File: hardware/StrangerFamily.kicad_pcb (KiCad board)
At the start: 2 copper layers, 34.5 x 45.5 mm, 8 parts, among them J2 Power_LEDs, J3 Output_LEDs, P1 CONN_13X2, U1 TXB0104PW

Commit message: 2 channels, cleanup
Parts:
- removed C3, C4: 10u, Capacitor_SMD:C_0805_2012Metric_Pad1.15x1.40mm_HandSolder
- added J4: Output_LED_MOSI, Connector_JST:JST_XH_S03B-XH-A-1_1x03_P2.50mm_Horizontal, F.Cu at (151.2, 137.0)
- J3: value Output_LEDs -> Output_LED_PWM
- moved C1 21.8 mm to (164.5, 137.0)
- moved C2 21.8 mm to (164.5, 143.0)
- moved U1 21.8 mm to (158.8, 140.0)
- moved J2 16.1 mm to (148.5, 160.0), turned to 0 degrees
- moved J3 12.5 mm to (151.2, 148.0)
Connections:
- U1 pad 3: Net-(U1-Pad3) -> /GPIO10(MOSI)
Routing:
- net GND: track 98.8 -> 34.6 mm
- net /GPIO18: track 32.3 -> 9.97 mm
- net +3V3: track 39.2 -> 18.1 mm
- net VDD: track 34.0 -> 49.7 mm
- net /GPIO10(MOSI): track 0.00 -> 14.7 mm, vias 0 -> 1
- net Net-(J4-Pad2): track 0.00 -> 10.9 mm
- net +5V: track 13.2 -> 2.54 mm
- added copper zone on B.Cu, net GND
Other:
- outline, holes or cut-outs redrawn

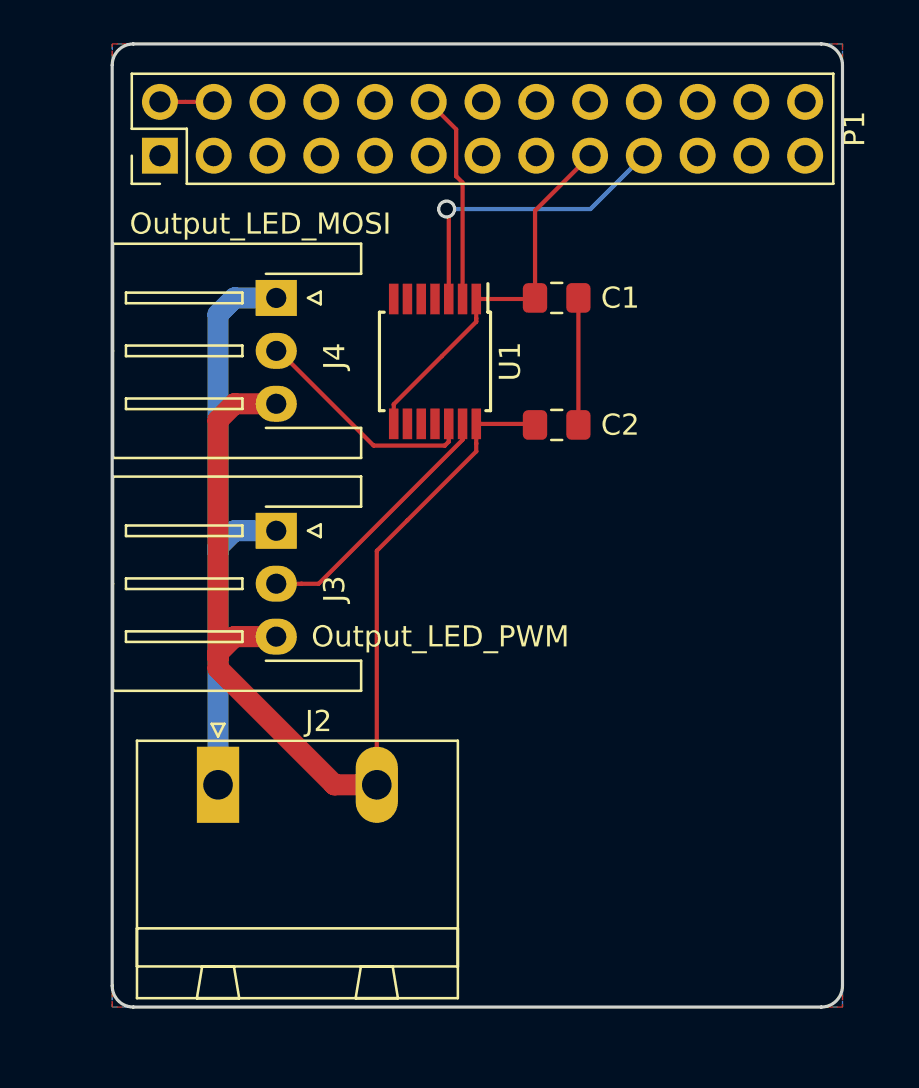
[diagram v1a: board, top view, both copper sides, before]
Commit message: Add LCD connector.
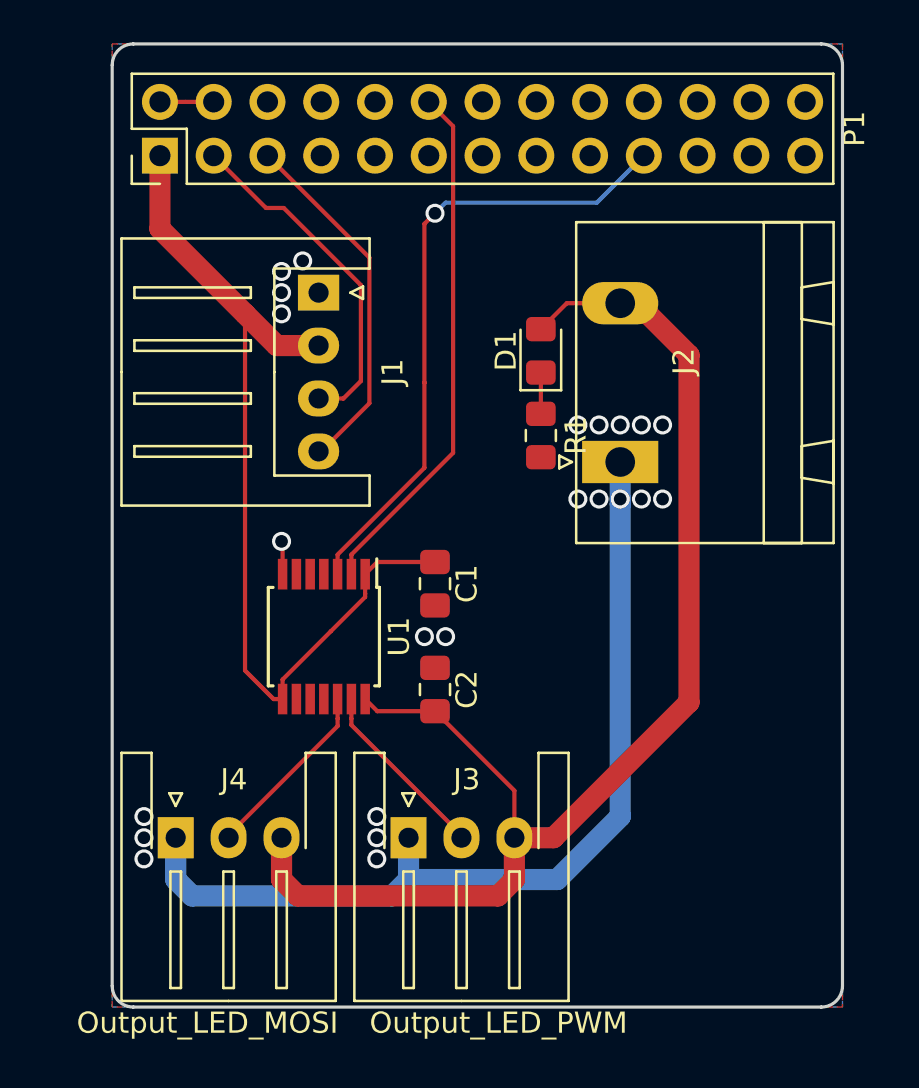
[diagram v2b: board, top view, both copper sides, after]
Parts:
- added D1: D, Diode_SMD:D_0805_2012Metric_Pad1.15x1.40mm_HandSolder, F.Cu at (163.8, 139.5)
- added J1: LCD_Conn, Connector_JST:JST_XH_S04B-XH-A_1x04_P2.50mm_Horizontal, F.Cu at (153.2, 136.8)
- added R1: R, Resistor_SMD:R_0805_2012Metric_Pad1.15x1.40mm_HandSolder, F.Cu at (163.8, 143.5)
- moved J4 25.9 mm to (146.5, 162.5), turned to 0 degrees
- moved J2 24.4 mm to (167.5, 144.8), turned to 90 degrees
- moved J3 15.8 mm to (157.5, 162.5), turned to 0 degrees
- moved C1 14.7 mm to (158.8, 150.5), turned to 90 degrees
- moved U1 14.0 mm to (153.5, 153.0)
- moved C2 13.8 mm to (158.8, 155.5), turned to 270 degrees
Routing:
- net +3V3: track 18.1 -> 43.5 mm
- net /GPIO1(SCL): track 0.00 -> 17.0 mm
- net /GPIO0(SDA): track 0.00 -> 16.4 mm
- net /GPIO10(MOSI): track 14.7 -> 29.9 mm
- net /GPIO18: track 9.97 -> 24.8 mm
- net VDD: track 49.7 -> 62.5 mm
- net GND: track 34.6 -> 45.1 mm, vias 0 -> 23
- net Net-(J3-Pad2): track 12.4 -> 8.70 mm
- net Net-(J4-Pad2): track 10.9 -> 8.68 mm
- net Net-(D1-Pad1): track 0.00 -> 1.95 mm

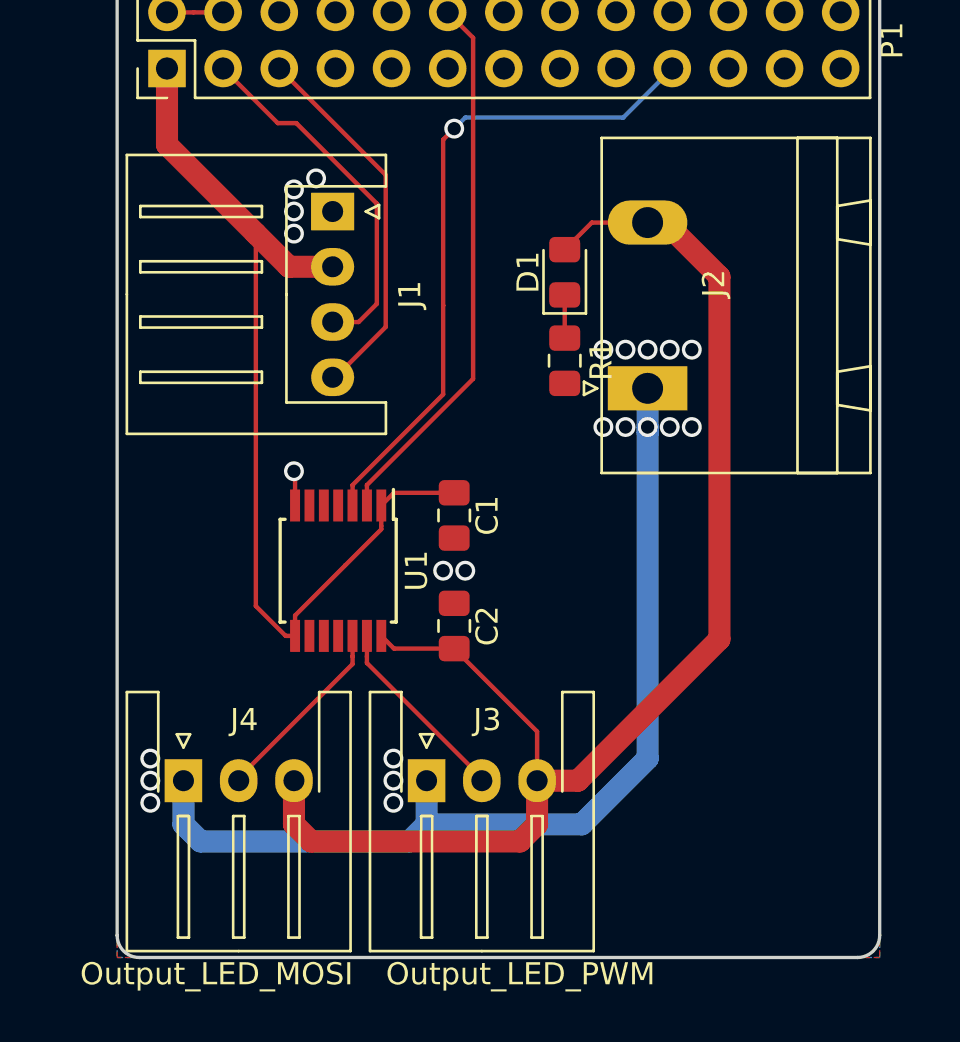
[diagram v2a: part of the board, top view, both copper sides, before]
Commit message: Change connector footprints (very small non critical changes)
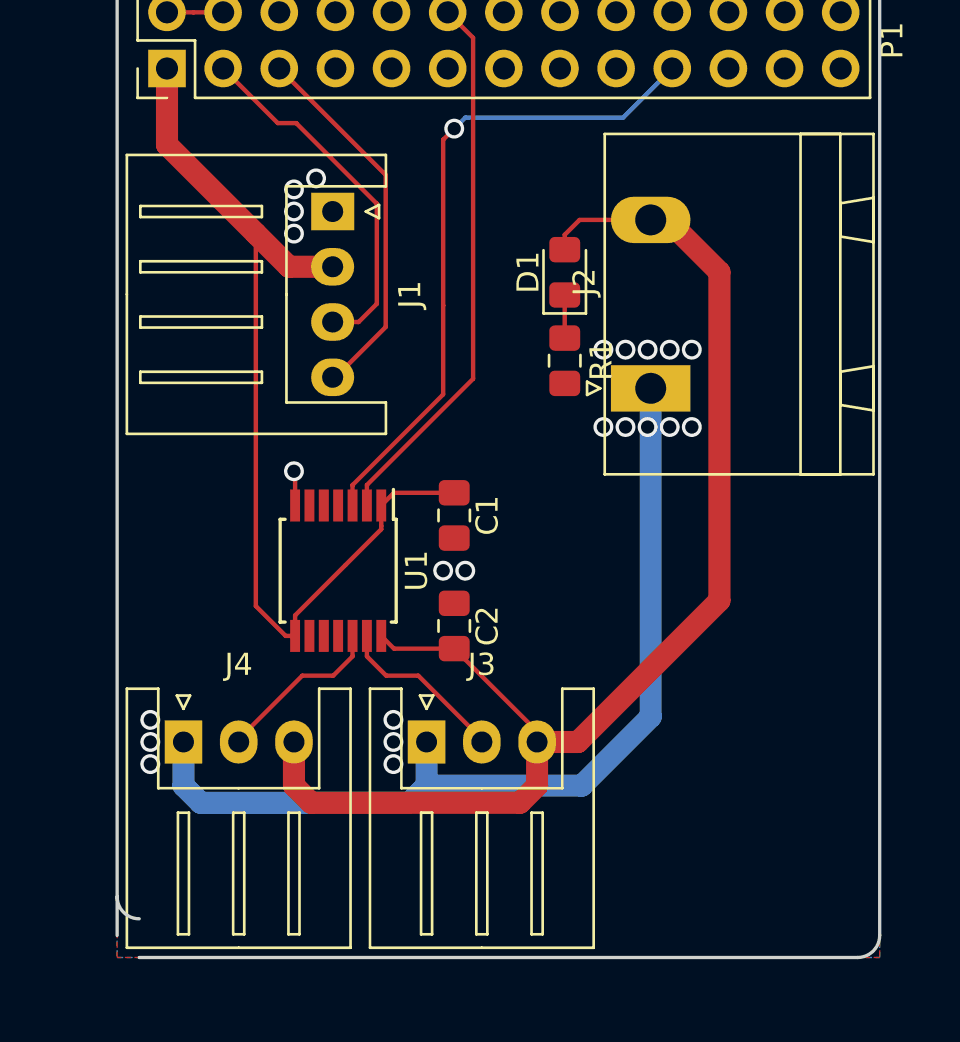
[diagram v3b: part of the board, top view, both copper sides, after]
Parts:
- J2: footprint Connector_Phoenix_GMSTB:PhoenixContact_GMSTBA_2,5_2-G_1x02_P7.50mm_Horizontal -> Connector_Phoenix_GMSTB:PhoenixContact_GMSTBA_2,5_2-G-7,62_1x02_P7.62mm_Horizontal
- J3, J4: footprint Connector_JST:JST_XH_S03B-XH-A-1_1x03_P2.50mm_Horizontal -> Connector_JST:JST_XH_S03B-XH-A_1x03_P2.50mm_Horizontal
- moved J3 1.75 mm to (157.5, 160.8)
- moved J4 1.75 mm to (146.5, 160.8)
- moved J2 0.14 mm to (167.6, 144.8)
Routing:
- net VDD: track 62.5 -> 59.6 mm
- net GND: track 45.1 -> 43.5 mm
- net Net-(J4-Pad2): track 8.68 -> 7.75 mm
- net Net-(J3-Pad2): track 8.70 -> 7.80 mm
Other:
- outline, holes or cut-outs redrawn

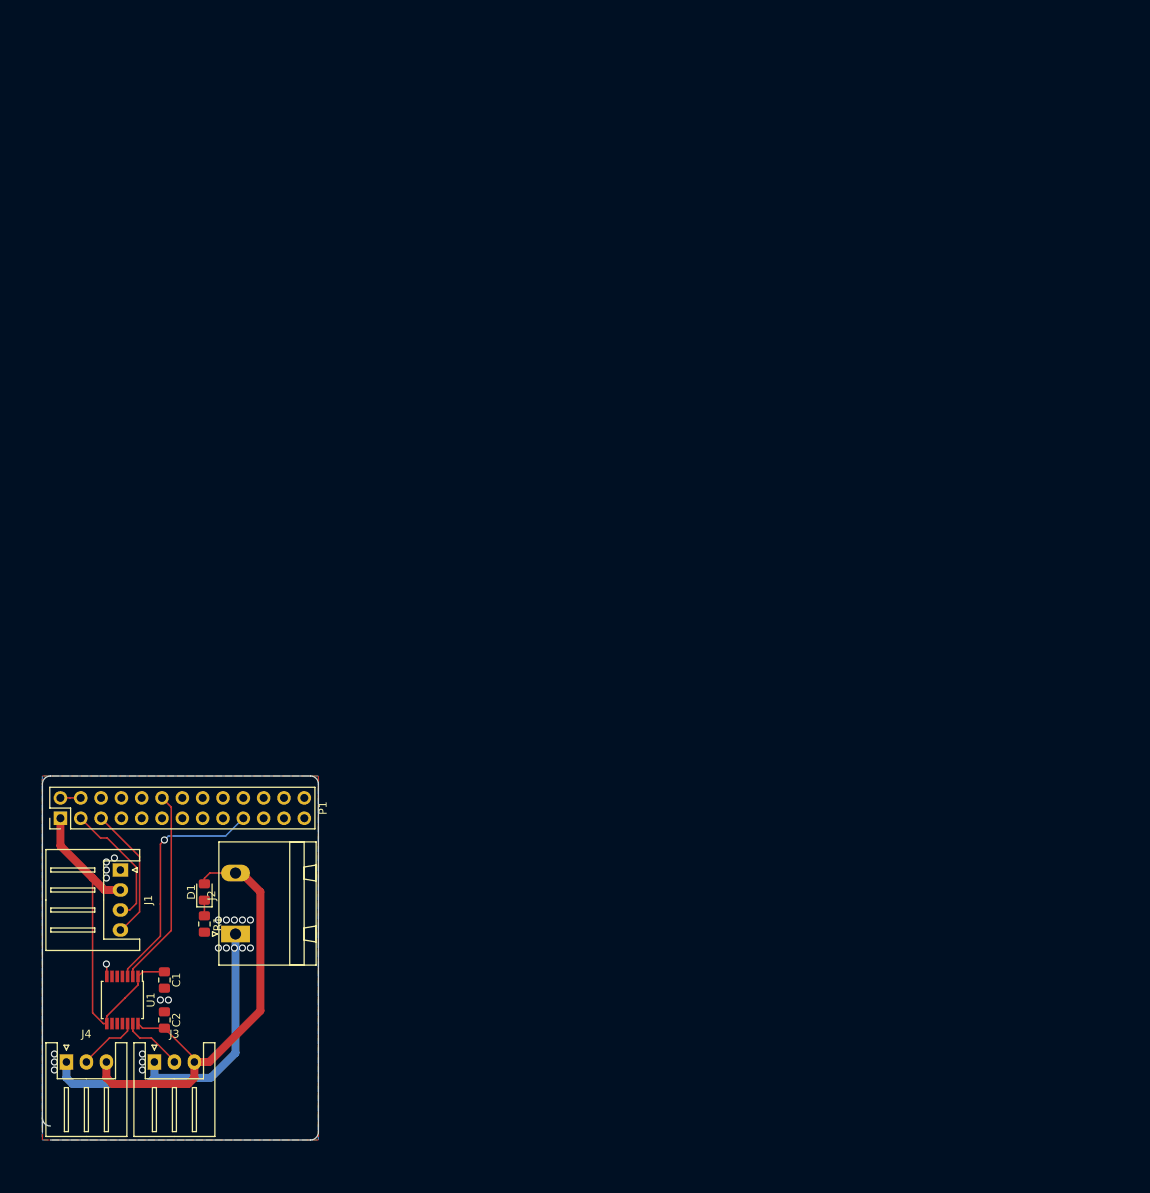
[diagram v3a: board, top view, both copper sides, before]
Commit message: v2 of hardware with rpi zero w, and arduino nano
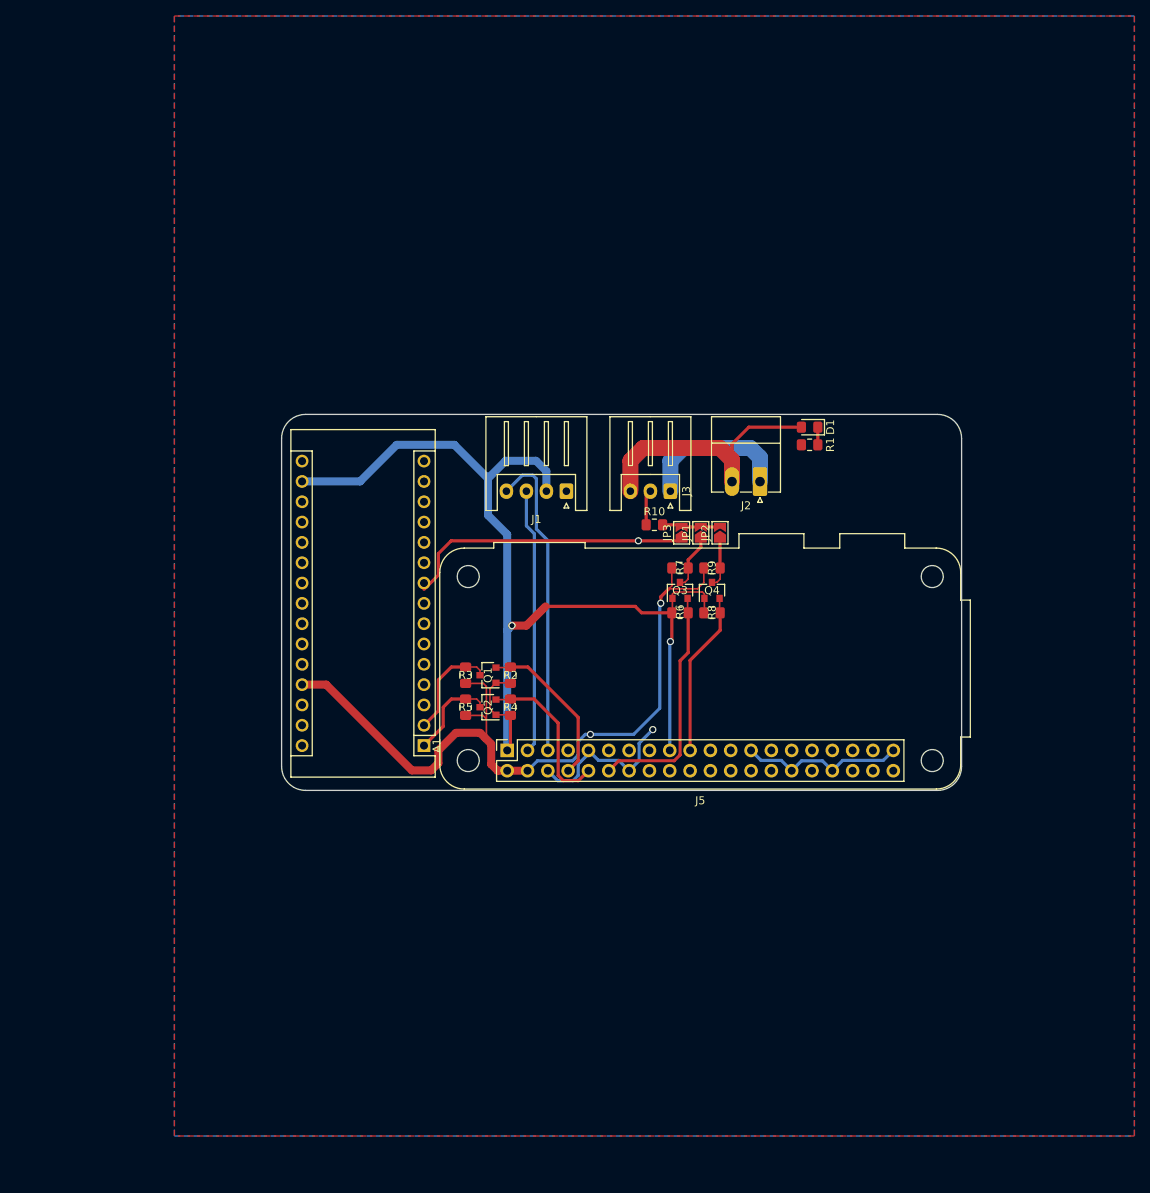
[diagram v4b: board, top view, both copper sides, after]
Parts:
- removed C1, C2: 100n, Capacitor_SMD:C_0805_2012Metric_Pad1.15x1.40mm_HandSolder
- removed J4: Output_LED_MOSI, Connector_JST:JST_XH_S03B-XH-A_1x03_P2.50mm_Horizontal
- removed P1: CONN_13X2, Connector_PinHeader_2.54mm:PinHeader_2x13_P2.54mm_Vertical
- removed U1: TXB0104PW, Package_SO:TSSOP-14_4.4x5mm_P0.65mm
- added A1: Arduino_Nano_v3.x, Module:Arduino_Nano, F.Cu at (191.2, 121.2)
- added J5: Raspberry_Pi_zero, Module:Raspberry_Pi_Zero_Socketed_THT_FaceDown_MountingHoles, F.Cu at (201.6, 121.8)
- added JP1: Jumper_NC, Jumper:SolderJumper-2_P1.3mm_Open_TrianglePad1.0x1.5mm, F.Cu at (225.8, 94.6)
- added JP2: Jumper_NC, Jumper:SolderJumper-2_P1.3mm_Open_TrianglePad1.0x1.5mm, F.Cu at (228.2, 94.6)
- added JP3: Jumper_NC, Jumper:SolderJumper-2_P1.3mm_Open_TrianglePad1.0x1.5mm, F.Cu at (223.4, 94.6)
- added Q1: BSS138, Package_TO_SOT_SMD:SOT-23, F.Cu at (199.2, 112.4)
- added Q2: BSS138, Package_TO_SOT_SMD:SOT-23, F.Cu at (199.2, 116.4)
- added Q3: BSS138, Package_TO_SOT_SMD:SOT-23, F.Cu at (223.2, 101.8)
- added Q4: BSS138, Package_TO_SOT_SMD:SOT-23, F.Cu at (227.2, 101.8)
- added R10: 470, Resistor_SMD:R_0805_2012Metric_Pad1.15x1.40mm_HandSolder, F.Cu at (220.0, 93.6)
- added R2: 10k, Resistor_SMD:R_0805_2012Metric_Pad1.15x1.40mm_HandSolder, F.Cu at (202.0, 112.4)
- added R3: 10k, Resistor_SMD:R_0805_2012Metric_Pad1.15x1.40mm_HandSolder, F.Cu at (196.4, 112.4)
- added R4: 10k, Resistor_SMD:R_0805_2012Metric_Pad1.15x1.40mm_HandSolder, F.Cu at (202.0, 116.4)
- added R5: 10k, Resistor_SMD:R_0805_2012Metric_Pad1.15x1.40mm_HandSolder, F.Cu at (196.4, 116.4)
- added R6: 10k, Resistor_SMD:R_0805_2012Metric_Pad1.15x1.40mm_HandSolder, F.Cu at (223.2, 104.6)
- added R7: 10k, Resistor_SMD:R_0805_2012Metric_Pad1.15x1.40mm_HandSolder, F.Cu at (223.2, 99.0)
- added R8: 10k, Resistor_SMD:R_0805_2012Metric_Pad1.15x1.40mm_HandSolder, F.Cu at (227.2, 104.6)
- added R9: 10k, Resistor_SMD:R_0805_2012Metric_Pad1.15x1.40mm_HandSolder, F.Cu at (227.2, 99.0)
- J1: footprint Connector_JST:JST_XH_S04B-XH-A_1x04_P2.50mm_Horizontal -> Connector_JST:JST_XH_S4B-XH-A_1x04_P2.50mm_Horizontal
- J2: footprint Connector_Phoenix_GMSTB:PhoenixContact_GMSTBA_2,5_2-G-7,62_1x02_P7.62mm_Horizontal -> Connector_Phoenix_MC:PhoenixContact_MC_1,5_2-G-3.5_1x02_P3.50mm_Horizontal
- J3: value Output_LED_PWM -> Output_LED; footprint Connector_JST:JST_XH_S03B-XH-A_1x03_P2.50mm_Horizontal -> Connector_JST:JST_XH_S3B-XH-A_1x03_P2.50mm_Horizontal
- moved R1 96.5 mm to (239.4, 83.6), turned to 180 degrees
- moved J3 96.2 mm to (222.0, 89.4), turned to 180 degrees
- moved D1 95.4 mm to (239.4, 81.4), turned to 180 degrees
- moved J2 86.6 mm to (233.2, 88.2), turned to 180 degrees
- moved J1 73.1 mm to (209.0, 89.4), turned to 180 degrees
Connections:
- J1 pad 3: /GPIO0(SDA) -> /LCD_SDA
- J1 pad 4: /GPIO1(SCL) -> /LCD_SLC
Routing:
- net +5V: track 2.54 -> 96.4 mm, vias 0 -> 2
- net +3V3: track 43.5 -> 134.4 mm, vias 0 -> 2
- net /LCD_SLC: track 0.00 -> 39.3 mm
- net /Arduino_out: track 0.00 -> 36.4 mm, vias 0 -> 1
- net /LCD_SDA: track 0.00 -> 33.2 mm
- net /GPIO10(MOSI): track 29.9 -> 0.00 mm, vias 1 -> 0
- net /PWM0: track 0.00 -> 29.7 mm
- net VDD: track 59.6 -> 32.0 mm
- net /GPIO18: track 24.8 -> 0.00 mm
- net /MOSI: track 0.00 -> 20.6 mm
- net /RPi_RX: track 0.00 -> 20.2 mm
- net /RPi_TX: track 0.00 -> 20.1 mm
- net GND: track 43.5 -> 60.8 mm, vias 23 -> 1
- net /GPIO1(SCL): track 17.0 -> 0.00 mm
- net /GPIO0(SDA): track 16.4 -> 0.00 mm
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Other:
- board size 34.5 x 45.5 mm -> 85 x 47 mm
- board text removed: "1/8" JACK OK WITH STD HEADERS !NO TH ABOVE!"
- board text removed: "DOUBLE USB CUTOUT FOR ALL BOARDS"
- board text removed: "RASPBERRY-PI ADDON BOARD VIEW FROM TOP NOTE: P1 SHOULD BE FITTED ON THE REVERSE OF THE BOARD"
- board text removed: "RCA REMOVE WITH STD HEADERS !NO TH ABOVE!"
- board text removed: "RJ45 CUTOUT FOR STD HEADERS !NO TH ABOVE!"

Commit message: Update hardware designs. This is v2 sent to prod in august 2020.
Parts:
- moved JP1 11.5 mm to (217.6, 86.6)
- moved JP3 11.5 mm to (215.2, 86.6)
- moved JP2 11.5 mm to (220.0, 86.6)
- moved Q3 10.9 mm to (215.0, 94.6)
- moved Q4 10.9 mm to (219.0, 94.6)
- moved R7 10.9 mm to (215.0, 91.8)
- moved R9 10.9 mm to (219.0, 91.8)
- moved R6 10.9 mm to (215.0, 97.4)
- moved R8 10.9 mm to (219.0, 97.4)
- moved D1 10.4 mm to (236.0, 71.6)
- moved J1 10.4 mm to (205.6, 79.6)
- moved J3 10.4 mm to (218.6, 79.6)
- moved R1 10.4 mm to (236.0, 73.8)
- moved R10 10.4 mm to (216.6, 83.8)
- moved J2 10.4 mm to (229.8, 78.4)
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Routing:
- net /PWM0: track 29.7 -> 25.2 mm
- net /Arduino_out: track 36.4 -> 32.1 mm, vias 1 -> 0
- net +5V: track 96.4 -> 92.5 mm
- net /LCD_SLC: track 39.3 -> 43.1 mm
- net /LCD_SDA: track 33.2 -> 36.5 mm
- net /MOSI_5V: track 6.26 -> 7.06 mm
- net /PWM0_5V: track 6.90 -> 7.70 mm
- net /MOSI: track 20.6 -> 19.9 mm
- net +3V3: track 134.4 -> 134.9 mm
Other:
- board size 85 x 47 mm -> 85 x 50 mm
